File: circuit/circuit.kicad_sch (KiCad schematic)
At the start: 3 parts

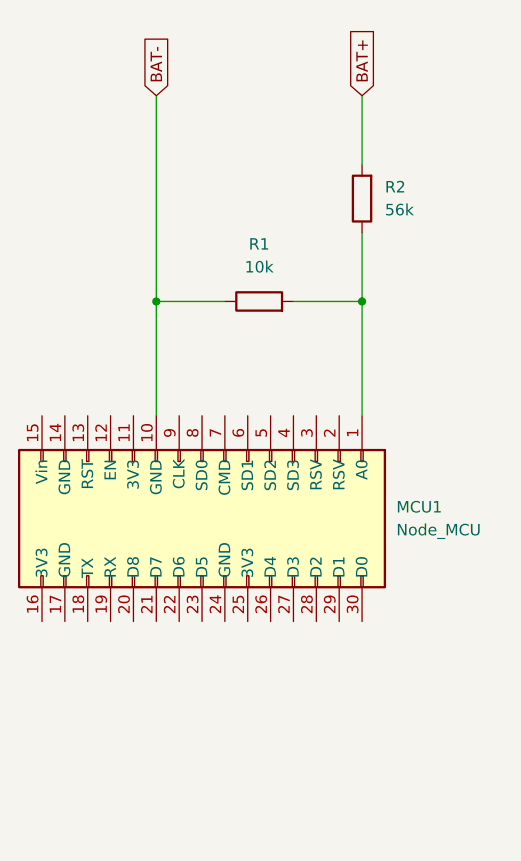
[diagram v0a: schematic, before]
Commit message: Add indicator LEDs to circuit schematic
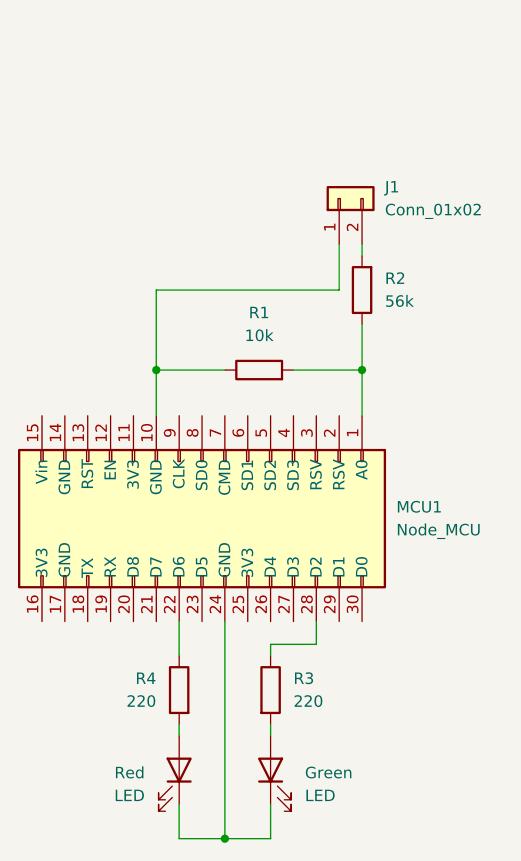
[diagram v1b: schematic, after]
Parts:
- added Green, Red: LED, symbol Device:LED
- added J1: Conn_01x02, symbol Connector_Generic:Conn_01x02
- added R3, R4: 220, symbol Device:R
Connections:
- net at MCU1.22 (D6): now also R4.1
- net at MCU1.24 (GND): now also Green.1 (K), Red.1 (K)
- net at MCU1.28 (D2): now also R3.1
- net BAT+: no longer names the net of R2.2
- net BAT+: now also J1.2 (Pin_2)
- net BAT-: no longer names the net of MCU1.10 (GND), R1.1
- net BAT-: now also J1.1 (Pin_1)
- new net: Green.2 (A), R3.2
- new net: R4.2, Red.2 (A)
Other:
- moved on the sheet: R1, R2
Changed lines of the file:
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@@
     (rev "V1")
   )
-  (junction (at 97.79 134.62) (diameter 0) (color 0 0 0 0)
-  )
-  (junction (at 120.65 134.62) (diameter 0) (color 0 0 0 0)
-  )
-  (wire (pts (xy 113.03 134.62) (xy 120.65 134.62))
-    (stroke (width 0) (type default))
-  )
-  (wire (pts (xy 105.41 134.62) (xy 97.79 134.62))
-    (stroke (width 0) (type default))
-  )
-  (wire (pts (xy 97.79 134.62) (xy 97.79 147.32))
-    (stroke (width 0) (type default))
-  )
-  (wire (pts (xy 97.79 111.76) (xy 97.79 134.62))
-    (stroke (width 0) (type default))
-  )
-  (wire (pts (xy 120.65 127) (xy 120.65 134.62))
-    (stroke (width 0) (type default))
-  )
-  (wire (pts (xy 120.65 134.62) (xy 120.65 147.32))
-    (stroke (width 0) (type default))
-  )
-  (wire (pts (xy 120.65 111.76) (xy 120.65 119.38))
-    (stroke (width 0) (type default))
-  )
-  (global_label "BAT-" (shape input) (at 97.79 111.76 90) (fields_autoplaced)
-    (effects (font (size 1.27 1.27)) (justify left))
-    (property "Intersheetrefs" "${INTERSHEET_REFS}" (at 97.79 103.8762 90)
-      (effects (font (size 1.27 1.27)) (justify left) hide)
-    )
-  )
-  (global_label "BAT+" (shape input) (at 120.65 111.76 90) (fields_autoplaced)
-    (effects (font (size 1.27 1.27)) (justify left))
-    (property "Intersheetrefs" "${INTERSHEET_REFS}" (at 120.65 103.8762 90)
-      (effects (font (size 1.27 1.27)) (justify left) hide)
-    )
-  )
-  (symbol (lib_id "Device:R") (at 109.22 134.62 90) (unit 1)
-    (in_bom yes) (on_board yes) (dnp no) (fields_autoplaced)
-    (property "Reference" "R1" (at 109.22 128.27 90)
+  (junction (at 97.79 142.24) (diameter 0) (color 0 0 0 0)
+  )
+  (junction (at 105.41 194.31) (diameter 0) (color 0 0 0 0)
+  )
+  (junction (at 120.65 142.24) (diameter 0) (color 0 0 0 0)
+  )
+  (wire (pts (xy 110.49 172.72) (xy 110.49 173.99))
+    (stroke (width 0) (type default))
+  )
+  (wire (pts (xy 115.57 172.72) (xy 115.57 170.18))
+    (stroke (width 0) (type default))
+  )
+  (wire (pts (xy 113.03 142.24) (xy 120.65 142.24))
+    (stroke (width 0) (type default))
+  )
+  (wire (pts (xy 105.41 194.31) (xy 110.49 194.31))
+    (stroke (width 0) (type default))
+  )
+  (wire (pts (xy 100.33 170.18) (xy 100.33 173.99))
+    (stroke (width 0) (type default))
+  )
+  (wire (pts (xy 110.49 172.72) (xy 115.57 172.72))
+    (stroke (width 0) (type default))
+  )
+  (wire (pts (xy 120.65 128.27) (xy 120.65 129.54))
+    (stroke (width 0) (type default))
+  )
+  (wire (pts (xy 100.33 194.31) (xy 105.41 194.31))
+    (stroke (width 0) (type default))
+  )
+  (wire (pts (xy 110.49 181.61) (xy 110.49 182.88))
+    (stroke (width 0) (type default))
+  )
+  (wire (pts (xy 100.33 181.61) (xy 100.33 182.88))
+    (stroke (width 0) (type default))
+  )
+  (wire (pts (xy 118.11 133.35) (xy 118.11 128.27))
+    (stroke (width 0) (type default))
+  )
+  (wire (pts (xy 105.41 142.24) (xy 97.79 142.24))
+    (stroke (width 0) (type default))
+  )
+  (wire (pts (xy 97.79 142.24) (xy 97.79 147.32))
+    (stroke (width 0) (type default))
+  )
+  (wire (pts (xy 100.33 190.5) (xy 100.33 194.31))
+    (stroke (width 0) (type default))
+  )
+  (wire (pts (xy 120.65 137.16) (xy 120.65 142.24))
+    (stroke (width 0) (type default))
+  )
+  (wire (pts (xy 105.41 170.18) (xy 105.41 194.31))
+    (stroke (width 0) (type default))
+  )
+  (wire (pts (xy 120.65 142.24) (xy 120.65 147.32))
+    (stroke (width 0) (type default))
+  )
+  (wire (pts (xy 110.49 190.5) (xy 110.49 194.31))
+    (stroke (width 0) (type default))
+  )
+  (wire (pts (xy 97.79 133.35) (xy 97.79 142.24))
+    (stroke (width 0) (type default))
+  )
+  (wire (pts (xy 97.79 133.35) (xy 118.11 133.35))
+    (stroke (width 0) (type default))
+  )
+  (symbol (lib_id "Device:R") (at 109.22 142.24 90) (unit 1)
+    (in_bom yes) (on_board yes) (dnp no) (fields_autoplaced)
+    (property "Reference" "R1" (at 109.22 135.89 90)
       (effects (font (size 1.27 1.27)))
     )
-    (property "Value" "10k" (at 109.22 130.81 90)
+    (property "Value" "10k" (at 109.22 138.43 90)
       (effects (font (size 1.27 1.27)))
     )
-    (property "Footprint" "" (at 109.22 136.398 90)
-      (effects (font (size 1.27 1.27)) hide)
-    )
-    (property "Datasheet" "~" (at 109.22 134.62 0)
+    (property "Footprint" "" (at 109.22 144.018 90)
+      (effects (font (size 1.27 1.27)) hide)
+    )
+    (property "Datasheet" "~" (at 109.22 142.24 0)
       (effects (font (size 1.27 1.27)) hide)
     )
@@
     )
   )
-  (symbol (lib_id "Device:R") (at 120.65 123.19 180) (unit 1)
-    (in_bom yes) (on_board yes) (dnp no) (fields_autoplaced)
-    (property "Reference" "R2" (at 123.19 121.92 0)
-      (effects (font (size 1.27 1.27)) (justify right))
-    )
-    (property "Value" "56k" (at 123.19 124.46 0)
-      (effects (font (size 1.27 1.27)) (justify right))
-    )
-    (property "Footprint" "" (at 122.428 123.19 90)
-      (effects (font (size 1.27 1.27)) hide)
-    )
-    (property "Datasheet" "~" (at 120.65 123.19 0)
+  (symbol (lib_id "Device:R") (at 120.65 133.35 180) (unit 1)
+    (in_bom yes) (on_board yes) (dnp no) (fields_autoplaced)
+    (property "Reference" "R2" (at 123.19 132.08 0)
+      (effects (font (size 1.27 1.27)) (justify right))
+    )
+    (property "Value" "56k" (at 123.19 134.62 0)
+      (effects (font (size 1.27 1.27)) (justify right))
+    )
+    (property "Footprint" "" (at 122.428 133.35 90)
+      (effects (font (size 1.27 1.27)) hide)
+    )
+    (property "Datasheet" "~" (at 120.65 133.35 0)
       (effects (font (size 1.27 1.27)) hide)
     )
@@
         (path "/48d291fd-c4bd-4ce5-94c5-7fd7d30f5b38"
           (reference "R2") (unit 1)
+        )
+      )
+    )
+  )
+  (symbol (lib_id "Device:LED") (at 110.49 186.69 90) (unit 1)
+    (in_bom yes) (on_board yes) (dnp no) (fields_autoplaced)
+    (property "Reference" "Green" (at 114.3 187.0075 90)
+      (effects (font (size 1.27 1.27)) (justify right))
+    )
+    (property "Value" "LED" (at 114.3 189.5475 90)
+      (effects (font (size 1.27 1.27)) (justify right))
+    )
+    (property "Footprint" "" (at 110.49 186.69 0)
+      (effects (font (size 1.27 1.27)) hide)
+    )
+    (property "Datasheet" "~" (at 110.49 186.69 0)
+      (effects (font (size 1.27 1.27)) hide)
+    )
+    (pin "1")
+    (pin "2")
+    (instances
+      (project "circuit"
+        (path "/48d291fd-c4bd-4ce5-94c5-7fd7d30f5b38"
+          (reference "Green") (unit 1)
+        )
+      )
+    )
+  )
+  (symbol (lib_id "Device:R") (at 110.49 177.8 0) (unit 1)
+    (in_bom yes) (on_board yes) (dnp no) (fields_autoplaced)
+    (property "Reference" "R3" (at 113.03 176.53 0)
+      (effects (font (size 1.27 1.27)) (justify left))
+    )
+    (property "Value" "220" (at 113.03 179.07 0)
+      (effects (font (size 1.27 1.27)) (justify left))
+    )
+    (property "Footprint" "" (at 108.712 177.8 90)
+      (effects (font (size 1.27 1.27)) hide)
+    )
+    (property "Datasheet" "~" (at 110.49 177.8 0)
+      (effects (font (size 1.27 1.27)) hide)
+    )
+    (pin "2")
+    (pin "1")
+    (instances
+      (project "circuit"
+        (path "/48d291fd-c4bd-4ce5-94c5-7fd7d30f5b38"
+          (reference "R3") (unit 1)
         )
       )
@@
         )
       )
+    )
+  )
+  (symbol (lib_id "Connector_Generic:Conn_01x02") (at 118.11 123.19 90) (unit 1)
+    (in_bom yes) (on_board yes) (dnp no) (fields_autoplaced)
+    (property "Reference" "J1" (at 123.19 121.92 90)
+      (effects (font (size 1.27 1.27)) (justify right))
+    )
+    (property "Value" "Conn_01x02" (at 123.19 124.46 90)
+      (effects (font (size 1.27 1.27)) (justify right))
+    )
+    (property "Footprint" "" (at 118.11 123.19 0)
+      (effects (font (size 1.27 1.27)) hide)
+    )
+    (property "Datasheet" "~" (at 118.11 123.19 0)
+      (effects (font (size 1.27 1.27)) hide)
+    )
+    (pin "1")
+    (pin "2")
+    (instances
+      (project "circuit"
+        (path "/48d291fd-c4bd-4ce5-94c5-7fd7d30f5b38"
+          (reference "J1") (unit 1)
+        )
+      )
+    )
+  )
+  (symbol (lib_id "Device:R") (at 100.33 177.8 0) (mirror y) (unit 1)
+    (in_bom yes) (on_board yes) (dnp no)
+    (property "Reference" "R4" (at 97.79 176.53 0)
+      (effects (font (size 1.27 1.27)) (justify left))
+    )
+    (property "Value" "220" (at 97.79 179.07 0)
+      (effects (font (size 1.27 1.27)) (justify left))
+    )
+    (property "Footprint" "" (at 102.108 177.8 90)
+      (effects (font (size 1.27 1.27)) hide)
+    )
+    (property "Datasheet" "~" (at 100.33 177.8 0)
+      (effects (font (size 1.27 1.27)) hide)
+    )
+    (pin "2")
+    (pin "1")
+    (instances
+      (project "circuit"
+        (path "/48d291fd-c4bd-4ce5-94c5-7fd7d30f5b38"
+          (reference "R4") (unit 1)
+        )
+      )
+    )
+  )
+  (symbol (lib_id "Device:LED") (at 100.33 186.69 270) (mirror x) (unit 1)
+    (in_bom yes) (on_board yes) (dnp no)
+    (property "Reference" "Red" (at 96.52 187.0075 90)
+      (effects (font (size 1.27 1.27)) (justify right))
+    )
+    (property "Value" "LED" (at 96.52 189.5475 90)
+      (effects (font (size 1.27 1.27)) (justify right))
+    )
+    (property "Footprint" "" (at 100.33 186.69 0)
+      (effects (font (size 1.27 1.27)) hide)
+    )
+    (property "Datasheet" "~" (at 100.33 186.69 0)
+      (effects (font (size 1.27 1.27)) hide)
+    )
+    (pin "2")
+    (pin "1")
+    (instances
+      (project "circuit"
+        (path "/48d291fd-c4bd-4ce5-94c5-7fd7d30f5b38"
+          (reference "Red") (unit 1)
+        )
+      )
